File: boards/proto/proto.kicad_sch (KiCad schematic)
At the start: 4 parts, among them J1 XBUS_02, J2 PIA_INT, J3 VIA_INT, J4 ACIA_INT

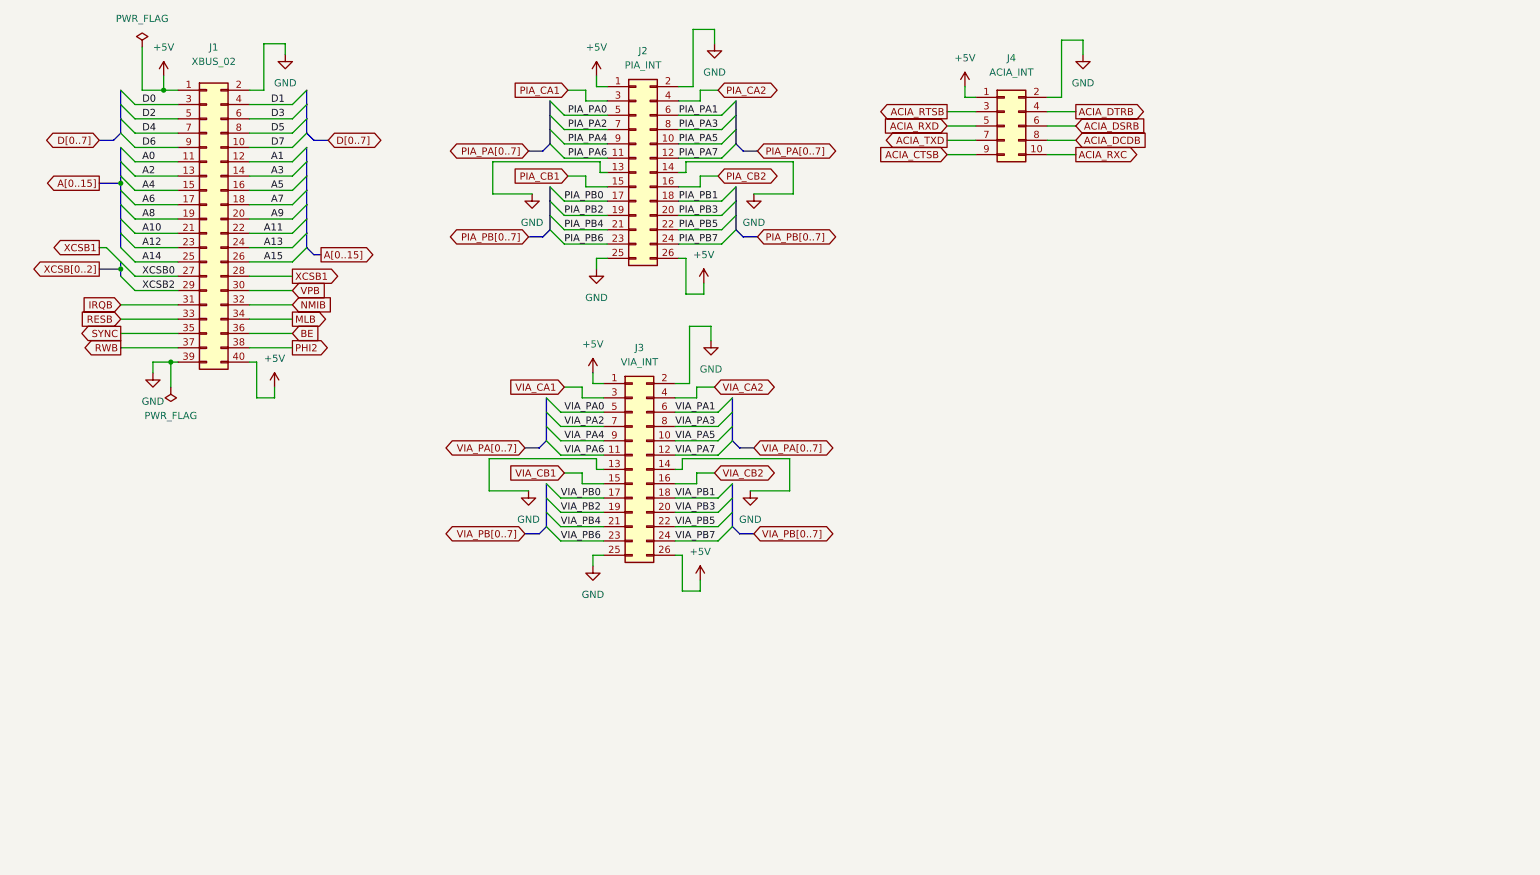
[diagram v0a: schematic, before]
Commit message: Create symbol for prototype area to break out connectors.
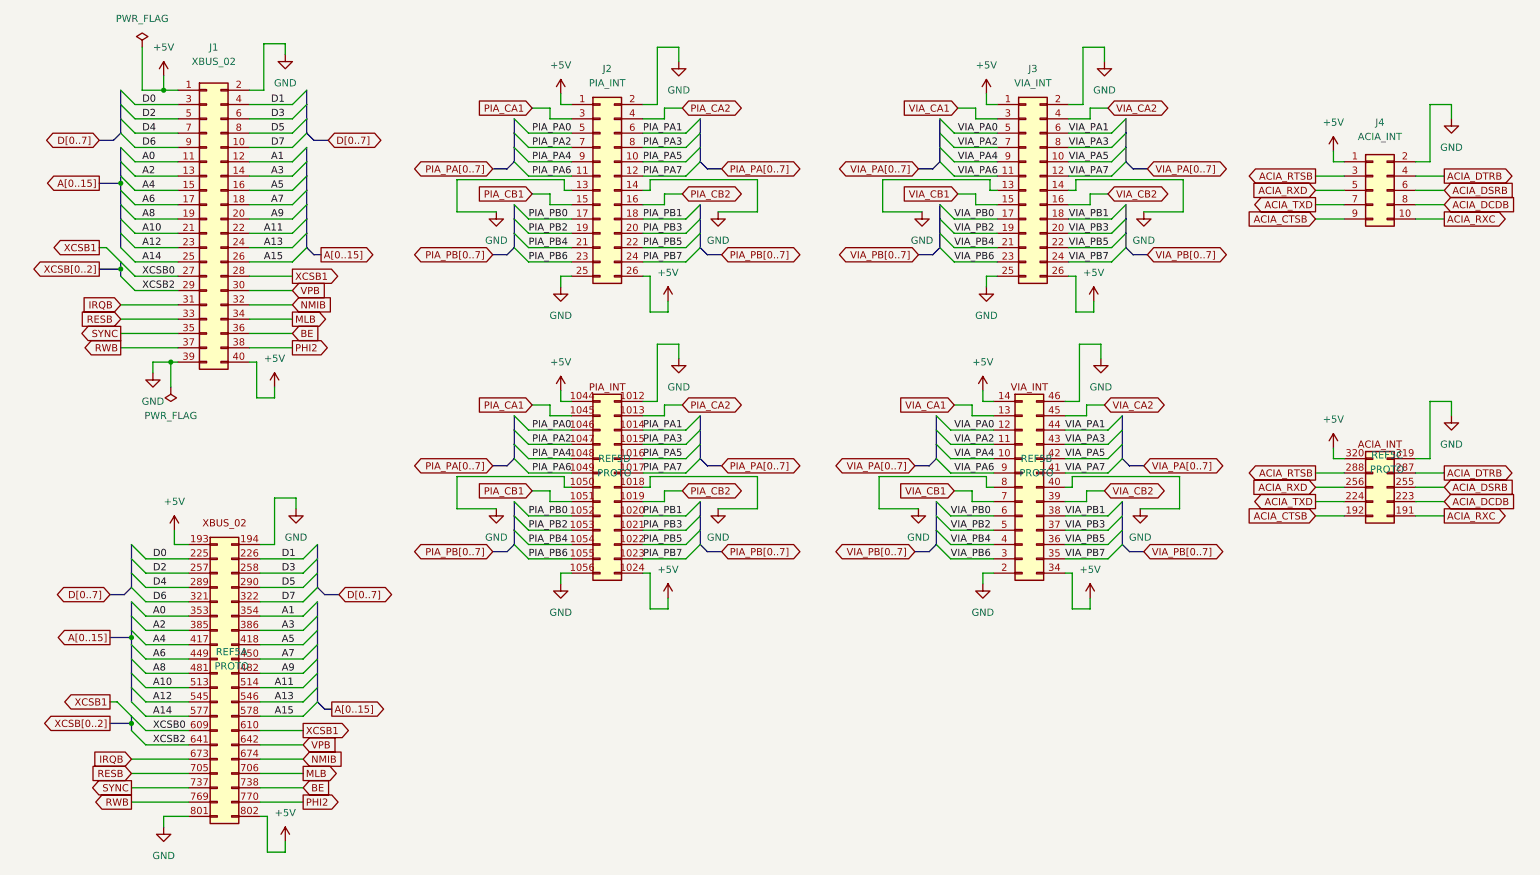
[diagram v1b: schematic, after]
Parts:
- added REF5: PROTO, proto:Prototype Area, symbol proto:Prototype_Area_Breakout
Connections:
- net +5V: now also REF5.1024 (Pin_26), REF5.1044 (Pin_1), REF5.14 (Pin_1), REF5.193 (Pin_1), REF5.320 (Pin_1), REF5.34 (Pin_26), REF5.802 (Pin_40)
- net A0: now also REF5.353 (Pin_11)
- net A1: now also REF5.354 (Pin_12)
- net A10: now also REF5.513 (Pin_21)
- net A11: now also REF5.514 (Pin_22)
- net A12: now also REF5.545 (Pin_23)
- net A13: now also REF5.546 (Pin_24)
- net A14: now also REF5.577 (Pin_25)
- net A15: now also REF5.578 (Pin_26)
- net A2: now also REF5.385 (Pin_13)
- net A3: now also REF5.386 (Pin_14)
- net A4: now also REF5.417 (Pin_15)
- net A5: now also REF5.418 (Pin_16)
- net A6: now also REF5.449 (Pin_17)
- net A7: now also REF5.450 (Pin_18)
- net A8: now also REF5.481 (Pin_19)
- net A9: now also REF5.482 (Pin_20)
- net ACIA_CTSB: now also REF5.192 (Pin_9)
- net ACIA_DCDB: now also REF5.223 (Pin_8)
- net ACIA_DSRB: now also REF5.255 (Pin_6)
- net ACIA_DTRB: now also REF5.287 (Pin_4)
- net ACIA_RTSB: now also REF5.288 (Pin_3)
- net ACIA_RXC: now also REF5.191 (Pin_10)
- net ACIA_RXD: now also REF5.256 (Pin_5)
- net ACIA_TXD: now also REF5.224 (Pin_7)
- net BE: now also REF5.738 (Pin_36)
- net D0: now also REF5.225 (Pin_3)
- net D1: now also REF5.226 (Pin_4)
- net D2: now also REF5.257 (Pin_5)
- net D3: now also REF5.258 (Pin_6)
- net D4: now also REF5.289 (Pin_7)
- net D5: now also REF5.290 (Pin_8)
- net D6: now also REF5.321 (Pin_9)
- net D7: now also REF5.322 (Pin_10)
- net GND: now also REF5.1012 (Pin_2), REF5.1018 (Pin_14), REF5.1050 (Pin_13), REF5.1056 (Pin_25), REF5.194 (Pin_2), REF5.2 (Pin_25), REF5.319 (Pin_2), REF5.40 (Pin_14), REF5.46 (Pin_2), REF5.8 (Pin_13), REF5.801 (Pin_39)
- net IRQB: now also REF5.673 (Pin_31)
- net MLB: now also REF5.706 (Pin_34)
- net NMIB: now also REF5.674 (Pin_32)
- net PHI2: now also REF5.770 (Pin_38)
- net PIA_CA1: now also REF5.1045 (Pin_3)
- net PIA_CA2: now also REF5.1013 (Pin_4)
- net PIA_CB1: now also REF5.1051 (Pin_15)
- net PIA_CB2: now also REF5.1019 (Pin_16)
- net PIA_PA0: now also REF5.1046 (Pin_5)
- net PIA_PA1: now also REF5.1014 (Pin_6)
- net PIA_PA2: now also REF5.1047 (Pin_7)
- net PIA_PA3: now also REF5.1015 (Pin_8)
- net PIA_PA4: now also REF5.1048 (Pin_9)
- net PIA_PA5: now also REF5.1016 (Pin_10)
- net PIA_PA6: now also REF5.1049 (Pin_11)
- net PIA_PA7: now also REF5.1017 (Pin_12)
- net PIA_PB0: now also REF5.1052 (Pin_17)
- net PIA_PB1: now also REF5.1020 (Pin_18)
- net PIA_PB2: now also REF5.1053 (Pin_19)
- net PIA_PB3: now also REF5.1021 (Pin_20)
- net PIA_PB4: now also REF5.1054 (Pin_21)
- net PIA_PB5: now also REF5.1022 (Pin_22)
- net PIA_PB6: now also REF5.1055 (Pin_23)
- net PIA_PB7: now also REF5.1023 (Pin_24)
- net RESB: now also REF5.705 (Pin_33)
- net RWB: now also REF5.769 (Pin_37)
- net SYNC: now also REF5.737 (Pin_35)
- net VIA_CA1: now also REF5.13 (Pin_3)
- net VIA_CA2: now also REF5.45 (Pin_4)
- net VIA_CB1: now also REF5.7 (Pin_15)
- net VIA_CB2: now also REF5.39 (Pin_16)
- net VIA_PA0: now also REF5.12 (Pin_5)
- net VIA_PA1: now also REF5.44 (Pin_6)
- net VIA_PA2: now also REF5.11 (Pin_7)
- net VIA_PA3: now also REF5.43 (Pin_8)
- net VIA_PA4: now also REF5.10 (Pin_9)
- net VIA_PA5: now also REF5.42 (Pin_10)
- net VIA_PA6: now also REF5.9 (Pin_11)
- net VIA_PA7: now also REF5.41 (Pin_12)
- net VIA_PB0: now also REF5.6 (Pin_17)
- net VIA_PB1: now also REF5.38 (Pin_18)
- net VIA_PB2: now also REF5.5 (Pin_19)
- net VIA_PB3: now also REF5.37 (Pin_20)
- net VIA_PB4: now also REF5.4 (Pin_21)
- net VIA_PB5: now also REF5.36 (Pin_22)
- net VIA_PB6: now also REF5.3 (Pin_23)
- net VIA_PB7: now also REF5.35 (Pin_24)
- net VPB: now also REF5.642 (Pin_30)
- net XCSB0: now also REF5.609 (Pin_27)
- net XCSB1: now also REF5.610 (Pin_28)
- net XCSB2: now also REF5.641 (Pin_29)
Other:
- moved on the sheet: J2, J3, J4
